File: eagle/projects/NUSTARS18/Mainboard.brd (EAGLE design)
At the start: 95 x 47 mm, 8 parts

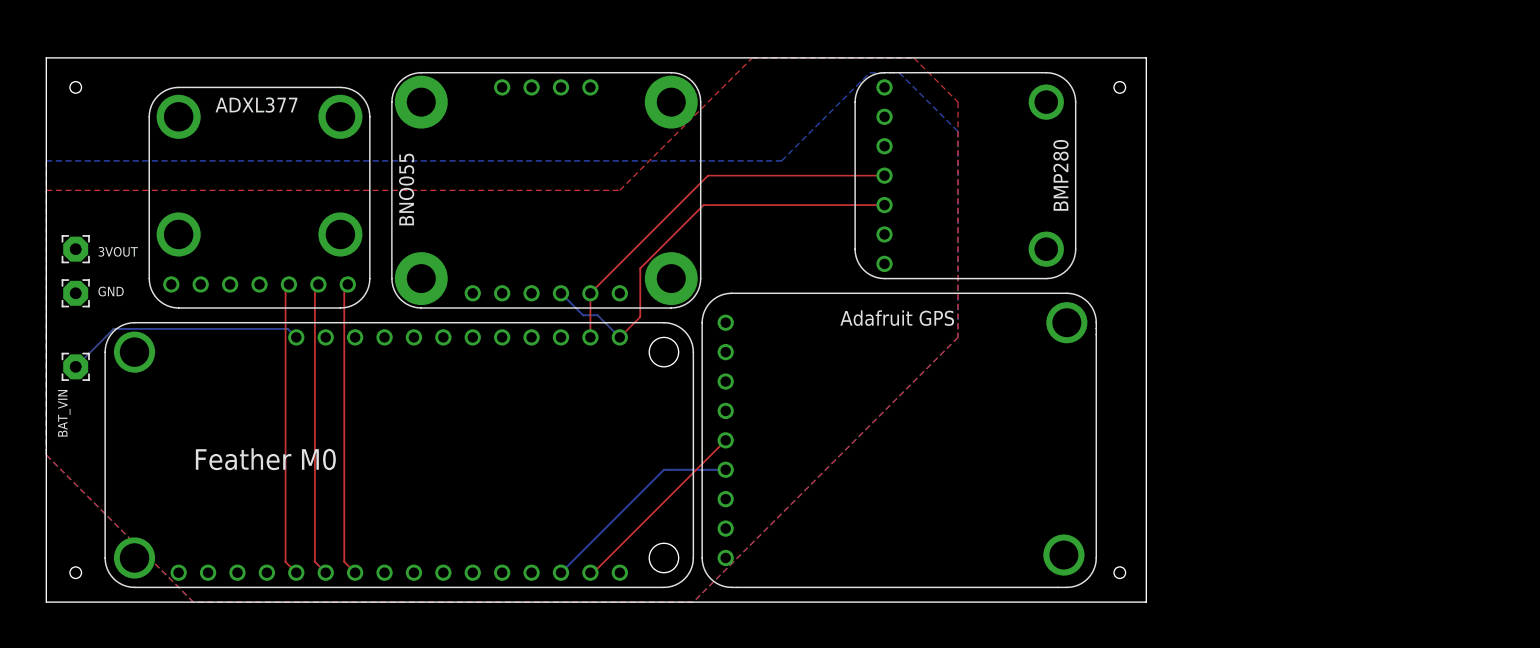
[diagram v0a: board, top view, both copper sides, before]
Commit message: Updated board to latest requirements
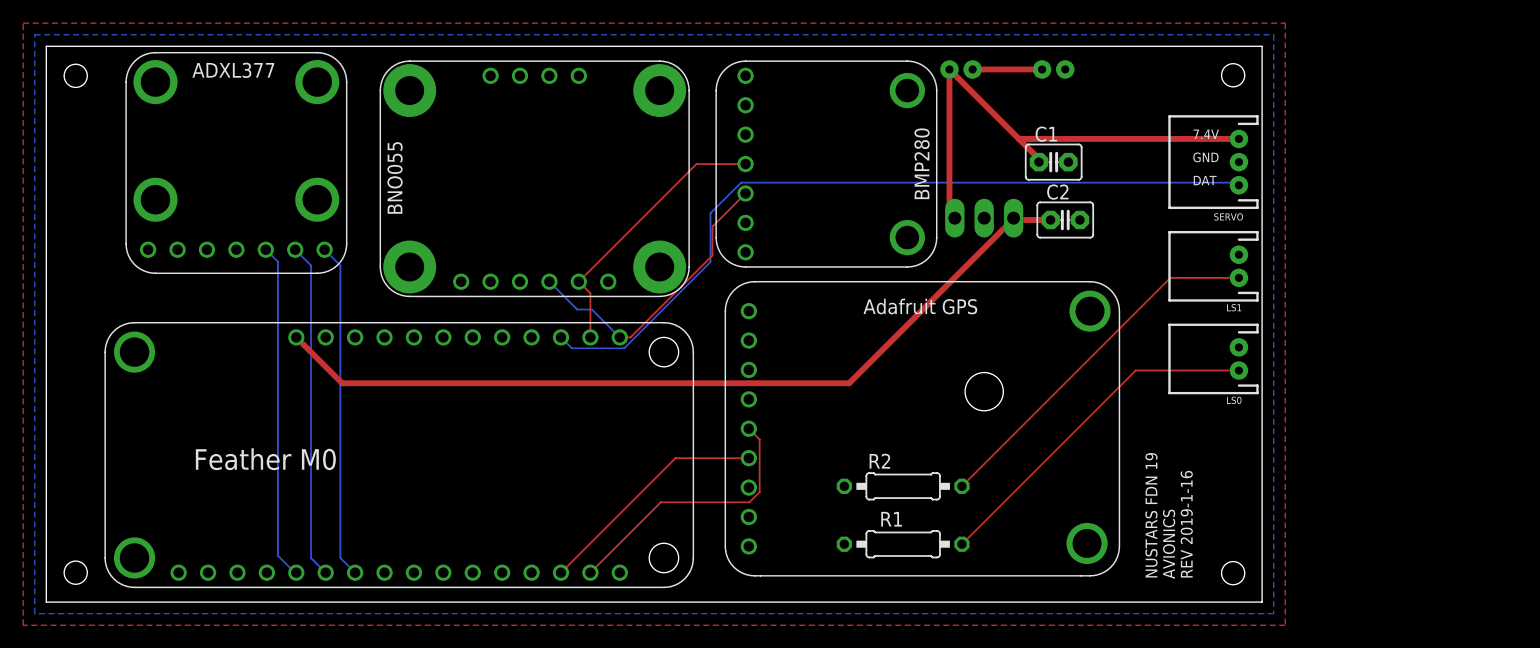
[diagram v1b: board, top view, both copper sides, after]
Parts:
- removed 3VOUT, BAT_VIN, GND: (no value), wirepad:2,15/1,0
- added BAT_0, BAT_1: (no value), SparkFun-Connectors:JST-2-PTH
- added C1, C2: (no value), capacitor-wima:C2.5-3
- added IC1: 7805T, linear:TO220H
- added LS0: HOME STOP, SparkFun-Connectors:JST-2-PTH
- added LS1: END STOP, SparkFun-Connectors:JST-2-PTH
- added R1, R2: 10k, rcl:0207/10
- added SERVO: (no value), SparkFun-Connectors:JST-3-PTH
- moved U$2 12.0 mm to (57.9, 46.7)
- moved U$3 3.61 mm to (6.89, 28.4)
- moved U$4 2.24 mm to (75.7, 15.0)
- moved U$5 1.41 mm to (42.2, 36.6)
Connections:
- removed net VCC: 3VOUT.1, U$1.3V, U$2.VIN, U$3.VIN, U$4.VIN, U$5.VIN
- new net 3V: R1.1, R2.1, U$1.3V, U$2.VIN, U$3.VIN, U$4.VIN, U$5.VIN
- new net 5V_REG: C2.1, IC1.3, U$1.BAT
- new net B_INT: BAT_0.2, BAT_1.1
- new net D_SERVO: SERVO.1, U$1.5
- new net LS0_D: LS0.1, R1.2
- new net LS1_D: LS1.1, R2.2
- net GND: now also BAT_1.2, C1.2, C2.2, IC1.2, LS0.2, LS1.2, SERVO.2; no longer GND.1, U$1.GND_0
- net V_BAT: now also BAT_0.1, C1.1, IC1.1, SERVO.3; no longer BAT_VIN.1, U$1.BAT
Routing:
- net 5V_REG: track 0.00 -> 72.8 mm
- net D_SERVO: track 0.00 -> 67.4 mm
- net LS1_D: track 0.00 -> 31.4 mm
- net LS0_D: track 0.00 -> 30.1 mm
- net V_BAT: track 20.7 -> 43.2 mm
- net DAT: track 36.7 -> 25.5 mm
- net CLK: track 33.4 -> 23.8 mm
- net TX: track 16.4 -> 23.4 mm
- net B_INT: track 0.00 -> 6.00 mm
- net ADXL_Z: track 25.4 -> 29.1 mm
- net ADXL_X: track 25.4 -> 29.0 mm
- net ADXL_Y: track 25.4 -> 29.0 mm
- net RX: track 17.9 -> 20.3 mm
- added copper zone on layer 1, net 3V
- removed copper zone on layer 1, net VCC
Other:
- board size 95 x 47 mm -> 105 x 48 mm
- board text added: "+3.7V"
- board text added: "7.4V"
- board text added: "DAT"
- board text added: "GND"
- board text added: "NUSTARS FDN 19 AVIONICS REV 2019-1-16"

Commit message: Updated the board yet again
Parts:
- removed IC1: 7805T, linear:TO220H
- added IC0: 7805T, linear:TO220H
- C1, C2: value (none) -> 10uF
- moved U$3 70.7 mm to (74.1, 6.40), flipped to the bottom
- moved BAT_0 59.5 mm to (123.0, 6.00), flipped to the top, turned to 90 degrees
- moved R1 55.8 mm to (27.0, 35.0)
- moved R2 55.2 mm to (27.0, 39.0)
- moved U$5 52.7 mm to (92.6, 21.2), flipped to the bottom, turned to 90 degrees
- moved BAT_1 48.2 mm to (123.0, 14.0), flipped to the top, turned to 90 degrees
- moved U$2 30.9 mm to (56.3, 15.8), turned to 0 degrees
- moved SERVO 25.0 mm to (123.0, 23.0)
- moved C2 24.0 mm to (111.0, 26.0), flipped to the bottom, turned to 270 degrees
- moved LS0 22.8 mm to (123.0, 32.0)
- moved LS1 22.8 mm to (123.0, 40.0)
- moved C1 22.5 mm to (106.0, 26.0), flipped to the bottom, turned to 90 degrees
- moved U$4 19.9 mm to (94.7, 21.0)
- moved U$1 9.85 mm to (16.3, 21.7)
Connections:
- removed net 5V_REG: C2.1, IC1.3, U$1.BAT
- new net 5V_REG_M0: C2.1, IC0.3, U$1.BAT
- net ADXL_X: now also U$1.A3; no longer U$1.A2
- net ADXL_Y: now also U$1.A2; no longer U$1.A1
- net ADXL_Z: now also U$1.A1; no longer U$1.A0
- net GND: now also IC0.2; no longer IC1.2
- net LS0_D: now also U$1.10
- net LS1_D: now also U$1.6
- net V_BAT: now also IC0.1; no longer IC1.1
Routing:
- net 5V_REG_M0: track 0.00 -> 103.4 mm
- net 5V_REG: track 72.8 -> 0.00 mm
- net LS1_D: track 31.4 -> 100.5 mm
- net LS0_D: track 30.1 -> 96.0 mm
- net CLK: track 23.8 -> 49.0 mm
- net D_SERVO: track 67.4 -> 90.1 mm
- net DAT: track 25.5 -> 47.8 mm
- net RX: track 20.3 -> 42.1 mm
- net TX: track 23.4 -> 43.6 mm
- net ADXL_Z: track 29.1 -> 43.2 mm
- net ADXL_X: track 29.0 -> 41.2 mm
- net ADXL_Y: track 29.0 -> 38.1 mm
- net V_BAT: track 43.2 -> 43.9 mm
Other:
- board size 105 x 48 mm -> 125 x 45 mm
- board text added: "NUSTARS FDN 19 AVIONICS REV 2019-1-18"
- board text removed: "+3.7V"
- board text removed: "NUSTARS FDN 19 AVIONICS REV 2019-1-16"

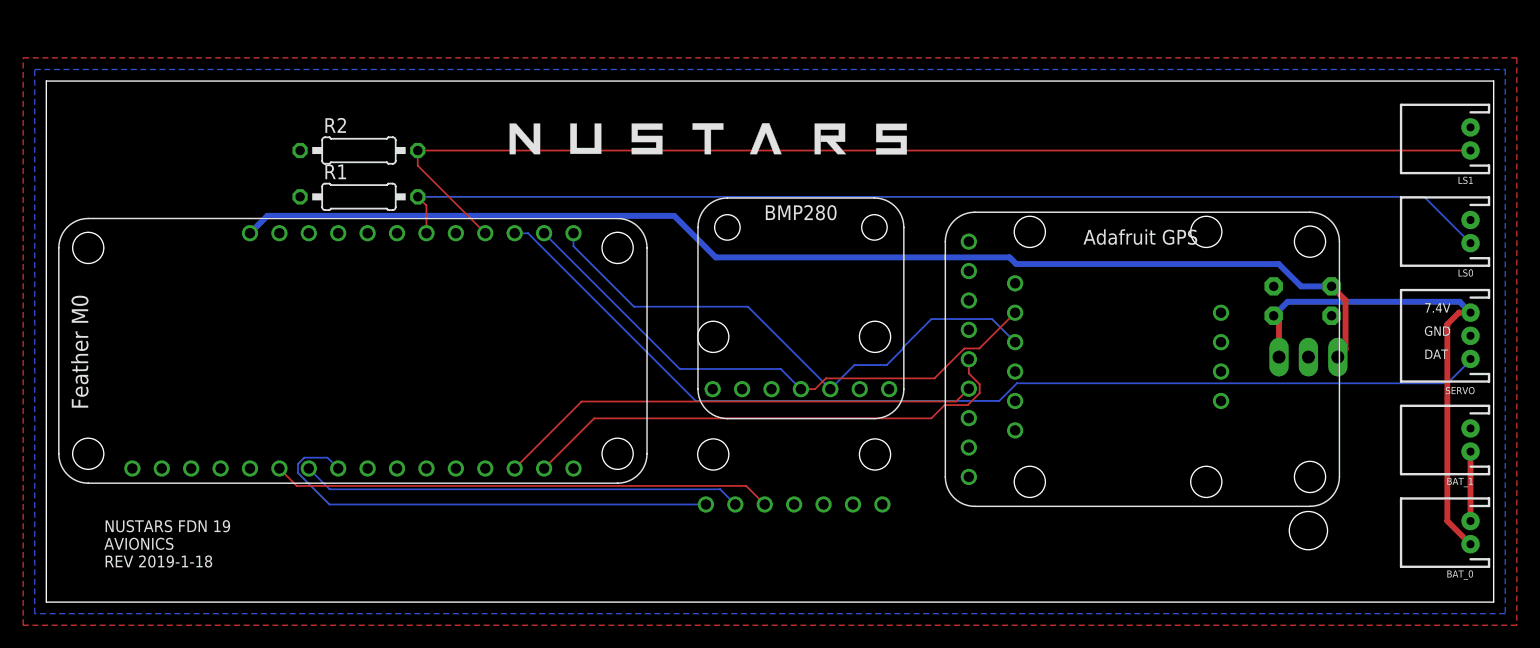
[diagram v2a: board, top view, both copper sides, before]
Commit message: Added Raven JST to board
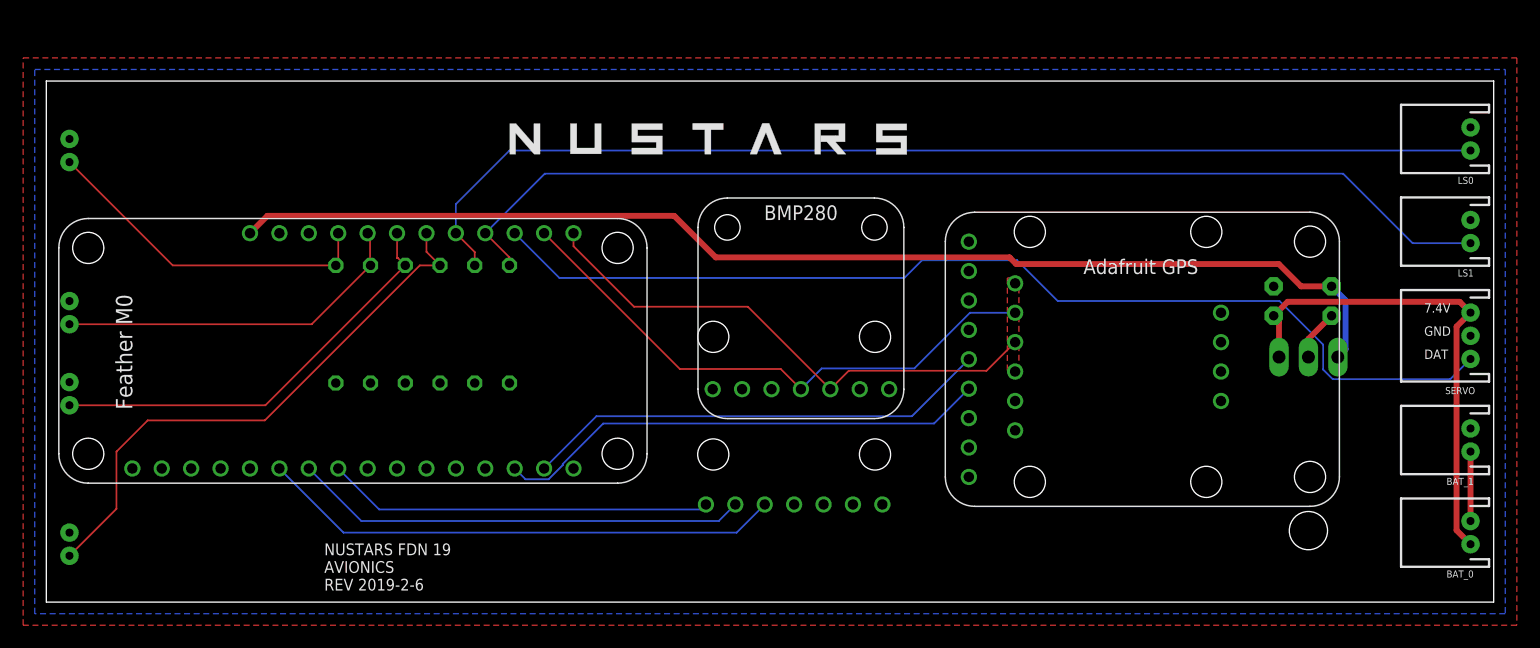
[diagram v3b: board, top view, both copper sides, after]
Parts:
- added R3, R4, R5, R6: 10k, rcl:0207/10
- added RAVEN_0A, RAVEN_0B, RAVEN_1A, RAVEN_1B: (no value), SparkFun-Connectors:JST-2-PTH
- moved R2 18.0 mm to (37.0, 24.0), flipped to the bottom, turned to 90 degrees
- moved R1 17.0 mm to (40.0, 24.0), flipped to the bottom, turned to 90 degrees
- moved LS0 8.00 mm to (123.0, 40.0)
- moved LS1 8.00 mm to (123.0, 32.0)
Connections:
- new net R0A_D: R3.1, RAVEN_0A.1, U$1.10
- new net R0B_D: R4.1, RAVEN_0B.1, U$1.11
- new net R1A_D: R5.1, RAVEN_1A.1, U$1.12
- new net R1B_D: R6.1, RAVEN_1B.1, U$1.13
- net 3V: now also R3.2, R4.2, R5.2, R6.2
- net GND: now also RAVEN_0A.2, RAVEN_0B.2, RAVEN_1A.2, RAVEN_1B.2
- net LS0_D: now also R2.2, U$1.9; no longer R1.2, U$1.10
- net LS1_D: now also R1.2; no longer R2.2
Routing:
- net R0A_D: track 0.00 -> 48.5 mm
- net R0B_D: track 0.00 -> 37.1 mm
- net R1A_D: track 0.00 -> 31.0 mm
- net R1B_D: track 0.00 -> 29.6 mm
- net ADXL_X: track 41.2 -> 33.4 mm
- net LS1_D: track 100.5 -> 93.4 mm
- net GND: track 0.00 -> 4.40 mm
- net TX: track 43.6 -> 40.6 mm
- net ADXL_Z: track 43.2 -> 45.2 mm
- net DAT: track 47.8 -> 46.1 mm
- net V_BAT: track 43.9 -> 42.6 mm
- net ADXL_Y: track 38.1 -> 39.3 mm
- net D_SERVO: track 90.1 -> 91.0 mm
- net RX: track 42.1 -> 42.9 mm
- net LS0_D: track 96.0 -> 95.5 mm
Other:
- board text added: "NUSTARS FDN 19 AVIONICS REV 2019-2-6"
- board text removed: "NUSTARS FDN 19 AVIONICS REV 2019-1-18"

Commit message: Added mass analysis and general board improvements
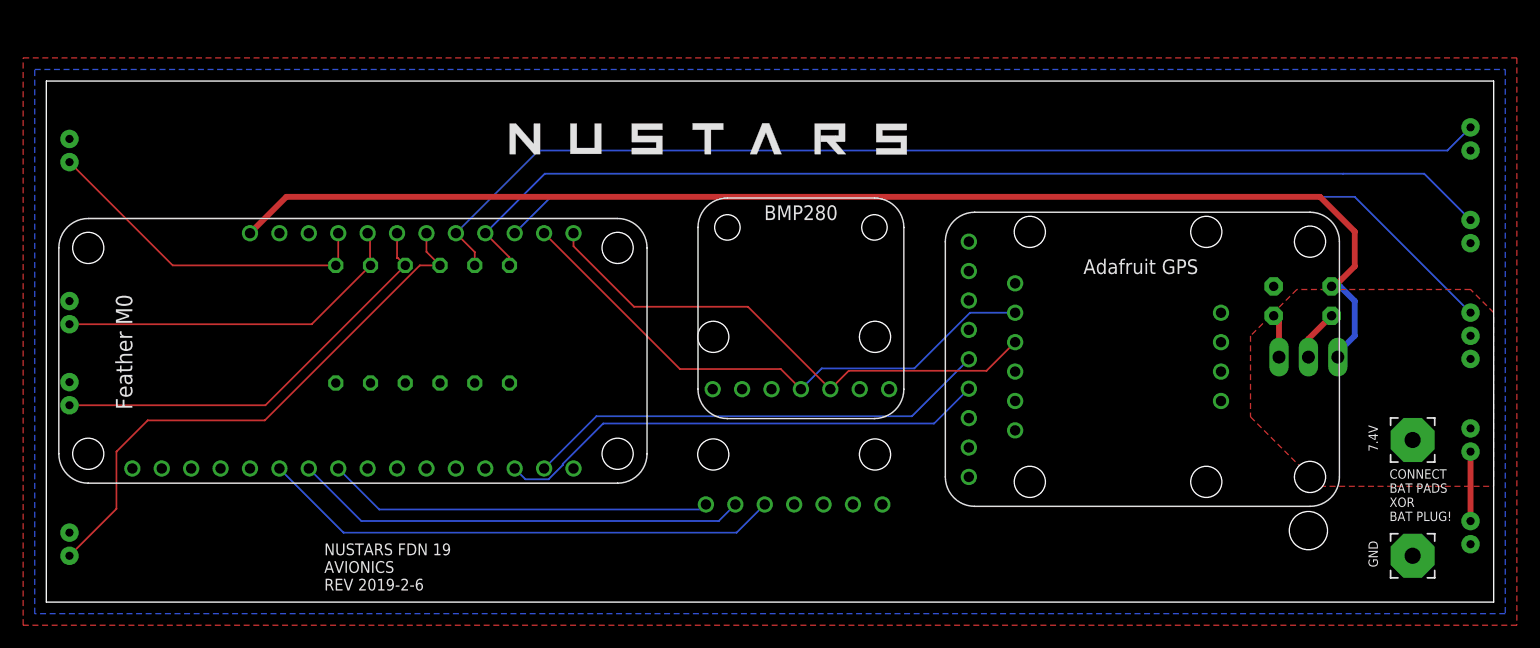
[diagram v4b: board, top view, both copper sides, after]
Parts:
- added BAT_7.4V, BAT_GND: (no value), wirepad:3,81/1,4
- moved BAT_0 8.00 mm to (123.0, 14.0), flipped to the bottom, turned to 270 degrees
- moved BAT_1 8.00 mm to (123.0, 6.00), flipped to the bottom, turned to 270 degrees
- flipped LS0 to the bottom, turned to 270 degrees
- flipped LS1 to the bottom, turned to 270 degrees
- flipped SERVO to the bottom, turned to 270 degrees
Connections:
- net GND: now also BAT_GND.1
- net V_BAT: now also BAT_7.4V.1
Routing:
- net V_BAT: track 42.6 -> 3.82 mm
- net 5V_REG_M0: track 103.4 -> 111.6 mm
- net D_SERVO: track 91.0 -> 88.0 mm
- net LS1_D: track 93.4 -> 92.5 mm
- net LS0_D: track 95.5 -> 94.9 mm
- added copper zone on layer 1, net V_BAT
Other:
- board text added: "3.7V"
- board text added: "< 7.4V"
- board text added: "< DAT"
- board text added: "< GND"
- board text added: "CONNECT BAT PADS XOR BAT PLUG!"
- board text added: "GND >"
- board text added: "Twenty G and I feel fine"
- board text removed: "DAT"
